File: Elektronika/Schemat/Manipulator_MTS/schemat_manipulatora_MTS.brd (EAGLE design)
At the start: 100 x 100 mm, 11 parts, among them IC1 MODUL_POLOLU, J1 XT60-M, U1 PRZETWORNICA

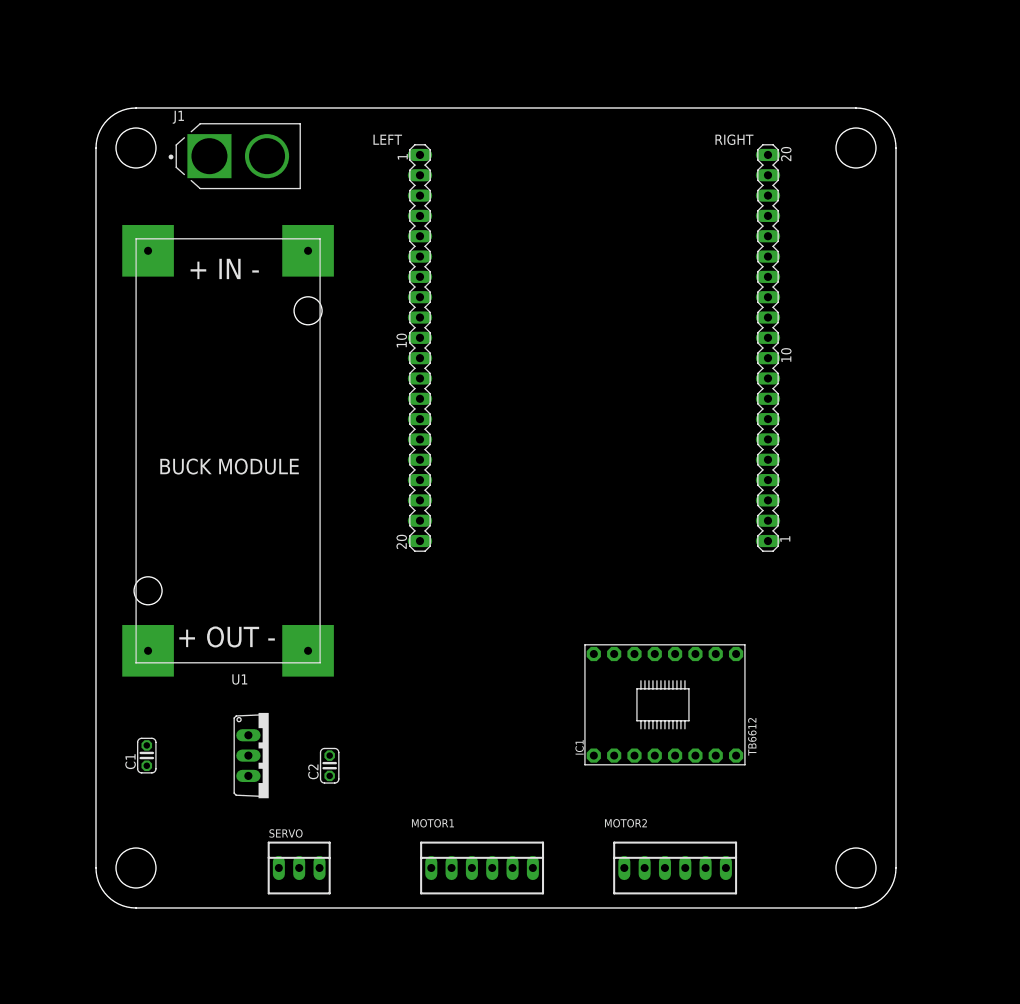
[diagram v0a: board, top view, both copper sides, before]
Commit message: v0.1.1
Dodano:
- w pełni stworzony model płytki PCB
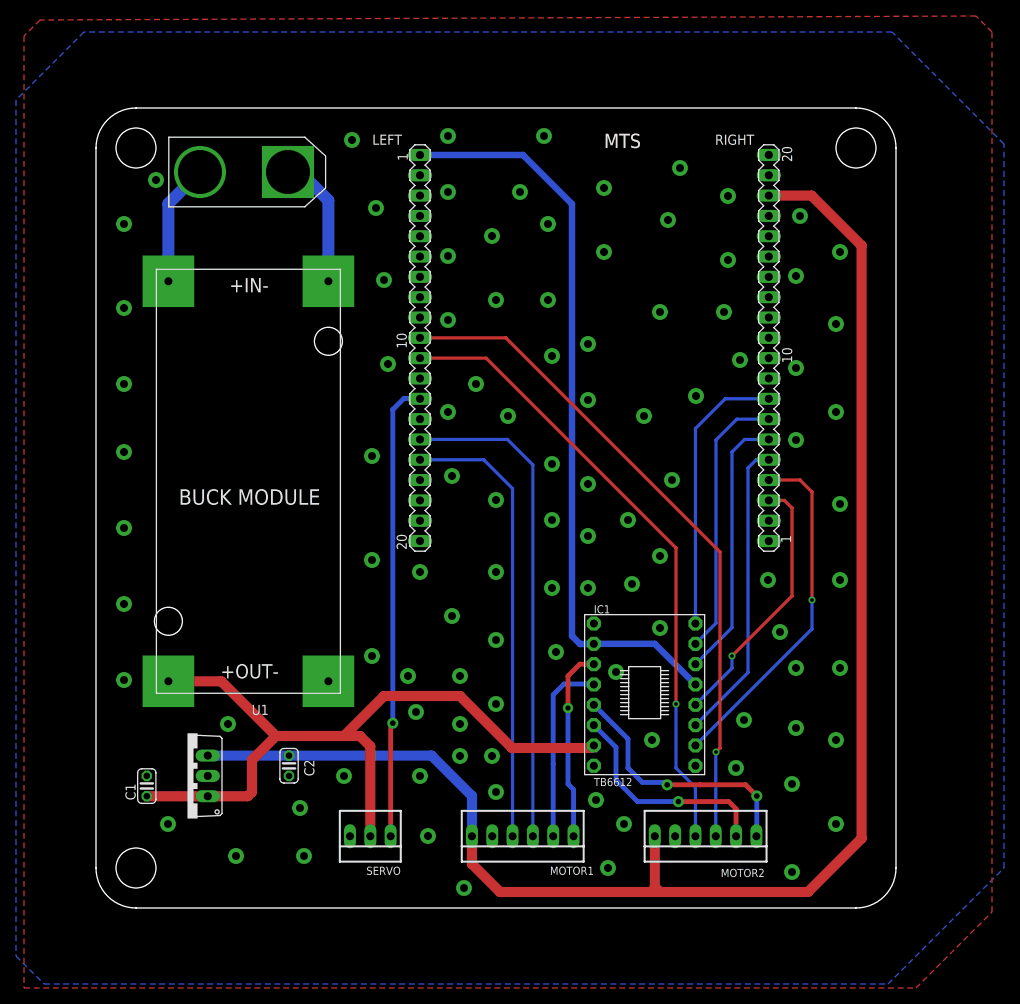
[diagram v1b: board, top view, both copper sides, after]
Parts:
- removed J1: XT60-M, XT60-M:AMASS_XT60-M
- added I1: XT90I-M, amy_library:XT90I-M
- moved LM7805CV 10.5 mm to (11.4, 16.5), turned to 90 degrees
- moved SERVO 9.74 mm to (34.3, 8.97), turned to 180 degrees
- moved MOTOR1 6.45 mm to (53.3, 8.97), turned to 180 degrees
- moved MOTOR2 5.50 mm to (76.2, 8.97), turned to 180 degrees
- moved C2 5.08 mm to (24.1, 17.8), turned to 270 degrees
- moved U1 4.58 mm to (19.1, 53.3)
- moved C1 3.81 mm to (6.35, 15.2)
- moved IC1 2.84 mm to (68.6, 26.7), turned to 0 degrees
- moved RIGHT 0.10 mm to (84.1, 70.0)
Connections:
- removed net 3V3: LEFT.1
- removed net 5V_I: RIGHT.18
- net +3.3V: now also LEFT.1
- net +5V: now also RIGHT.18
- net +6V: now also U1.4; no longer U1.3
- net ENC1_A1: now also LEFT.15; no longer LEFT.16
- net ENC1_B1: now also LEFT.16; no longer LEFT.15
- net GND: now also U1.3; no longer U1.4
- net N$1: now also I1.2, U1.2; no longer J1.2, U1.1
- net N$2: now also I1.1, U1.1; no longer J1.1, U1.2
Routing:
- net +5V: track 0.00 -> 192.1 mm
- net +6V: track 0.00 -> 97.6 mm
- net +3.3V: track 0.00 -> 93.5 mm
- net ENC2_A2: track 0.00 -> 84.3 mm, vias 0 -> 1
- net ENC2_B2: track 0.00 -> 78.9 mm, vias 0 -> 1
- net ENC1_A1: track 0.00 -> 61.8 mm
- net SERVO_PWM: track 0.00 -> 57.4 mm, vias 0 -> 1
- net ENC1_B1: track 0.00 -> 56.5 mm
- net PWMB: track 0.00 -> 43.7 mm, vias 0 -> 1
- net BIN2: track 0.00 -> 37.9 mm
- net PWMA: track 0.00 -> 35.1 mm
- net AIN2: track 0.00 -> 34.2 mm
- net AIN1: track 0.00 -> 33.7 mm
- net BIN1: track 0.00 -> 32.9 mm, vias 0 -> 1
- net MOTOR_2_1: track 0.00 -> 32.3 mm, vias 0 -> 2
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- added copper zone on layer 1, net GND
- added copper zone on layer 16, net GND
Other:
- board text added: "MTS"
